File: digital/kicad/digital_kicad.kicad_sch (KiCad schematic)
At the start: 27 parts, among them J1 Barrel_Jack_Switch, J2 Screw_Terminal_01x02, Q1 2N3904, Q2 2N3904, Q3 FDN340P, Q4 2N3904, SW1 SW_SPST, SW2 SW_Nidec_CAS-120A1

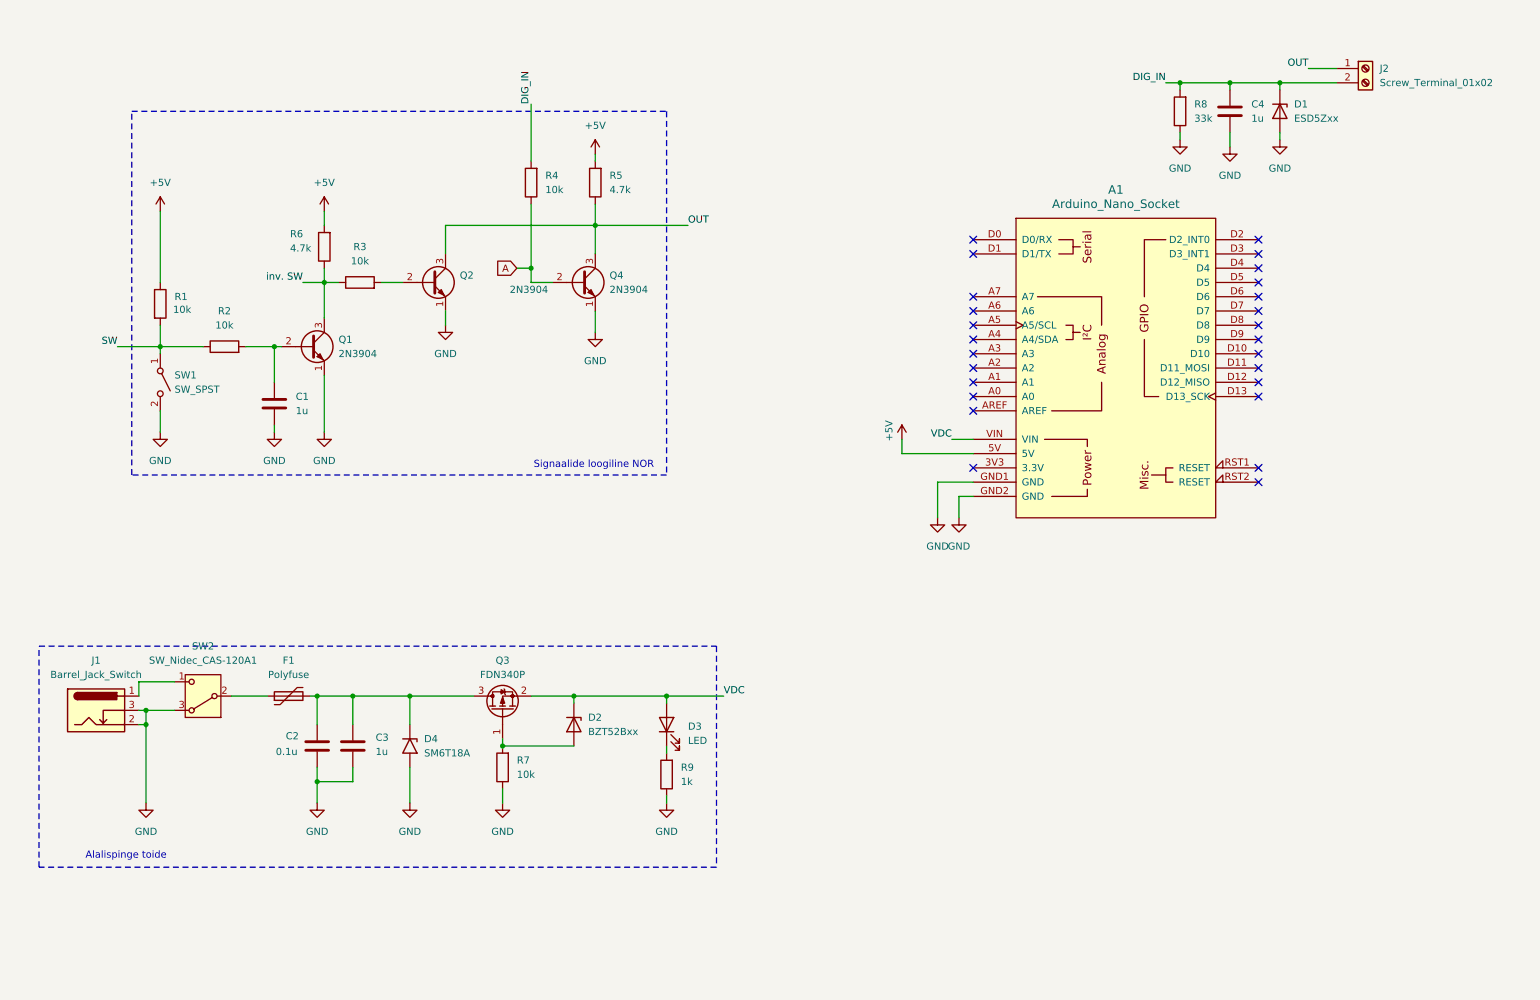
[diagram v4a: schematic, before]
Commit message: added bigger switch, slightly improved the NOR pcb circuit side track routing
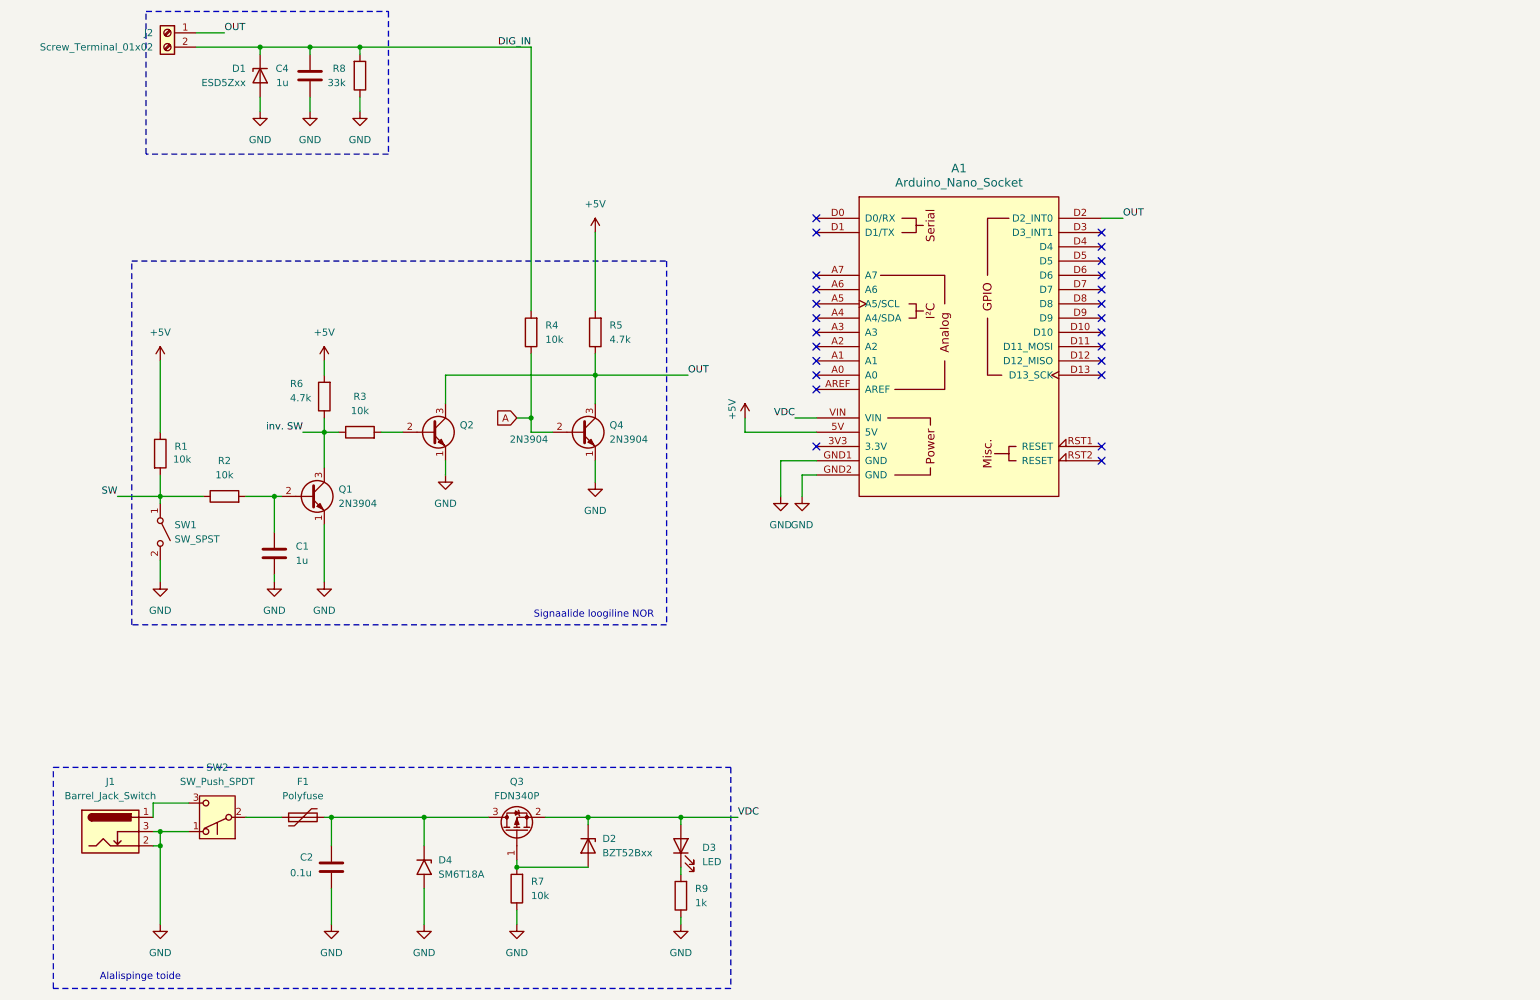
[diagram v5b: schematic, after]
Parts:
- removed C3: 1u, Capacitor_SMD:C_0805_2012Metric_Pad1.18x1.45mm_HandSolder, symbol Device:C
- removed SW2: SW_Nidec_CAS-120A1, Button_Switch_SMD:Nidec_Copal_CAS-120A, symbol Switch:SW_Nidec_CAS-120A1
- added SW2: SW_Push_SPDT, Button_Switch_THT:SW_Push_2P1T_Toggle_CK_PVA1xxH1xxxxxxV2, symbol Switch:SW_Push_SPDT
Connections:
- net GND: now also SW2.1 (A)
- net OUT: now also A1.D2 (D2_INT0)
- net at J1.1: now also SW2.3 (C)
- net at F1.1: now also SW2.2 (B)
- no-connect marks 26 -> 25
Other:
- moved on the sheet: A1, C1, C2, C4, D1, D2, D3, D4, F1, J1, J2, Q1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

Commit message: redid digital schematic to function as adapter, without arduino
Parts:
- removed A1: Arduino_Nano_Socket, PCM_arduino-library:Arduino_Nano_Socket, symbol PCM_arduino-library:Arduino_Nano_Socket
- removed F1: Polyfuse, Fuse:Fuse_1206_3216Metric_Pad1.42x1.75mm_HandSolder, symbol Device:Polyfuse
- removed J1: Barrel_Jack_Switch, Connector_BarrelJack:BarrelJack_Horizontal, symbol Connector:Barrel_Jack_Switch
- removed J2: Screw_Terminal_01x02, TerminalBlock_Phoenix:TerminalBlock_Phoenix_MKDS-1,5-2-5.08_1x02_P5.08mm_Horizontal, symbol Connector:Screw_Terminal_01x02
- removed SW2: SW_Push_SPDT, Button_Switch_THT:SW_Push_2P1T_Toggle_CK_PVA1xxH1xxxxxxV2, symbol Switch:SW_Push_SPDT
- added J1, J2, J3, J4: Conn_01x01_Pin, Connector_PinHeader_2.54mm:PinHeader_1x01_P2.54mm_Vertical, symbol Connector:Conn_01x01_Pin
- R7: value 10k -> 100k
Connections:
- net VDC is gone; now on net +5V: D2.1 (K), D3.2 (A), Q3.2 (S)
- net DIG_IN: now also J4.1 (Pin_1)
- net GND: now also J1.1 (Pin_1)
- net OUT: now also J3.1 (Pin_1)
- net DC_IN: now reaches C2.1, D4.1 (A1), Q3.3 (D)
- net DC_IN: now also J2.1 (Pin_1)
- no-connect marks 25 -> 0
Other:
- moved on the sheet: C1, C4, D1, Q1, Q2, Q4, R1, R2, R3, R4, R5, R6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

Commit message: sync latest adjustments for final presentation
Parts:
- removed D2: BZT52Bxx, Diode_SMD:D_SOD-123F, symbol Diode:BZT52Bxx
- removed R7: 100k, Resistor_SMD:R_0805_2012Metric_Pad1.20x1.40mm_HandSolder, symbol Device:R
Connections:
- net GND: now also Q3.1 (G)
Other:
- note added: "Digitaalse signaali sisend"
- title: (none) -> Arduino digisisendi laiend
- moved on the sheet: C1, C2, C4, D1, D3, D4, J1, J2, J3, J4, Q1, Q2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
